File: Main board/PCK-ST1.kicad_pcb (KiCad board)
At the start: 4 copper layers, 65 x 55.6 mm, 195 parts, among them IC1 DRV8434/24, IC2 DRV8434/24, IC3 DRV8434/24, IC4 DRV8434/24, IC5 TLV70033DDCR, IC7 TPS2121RUXR, IC8 TPS25730DREFR, J1 RPi, J10 RA, J11 EL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

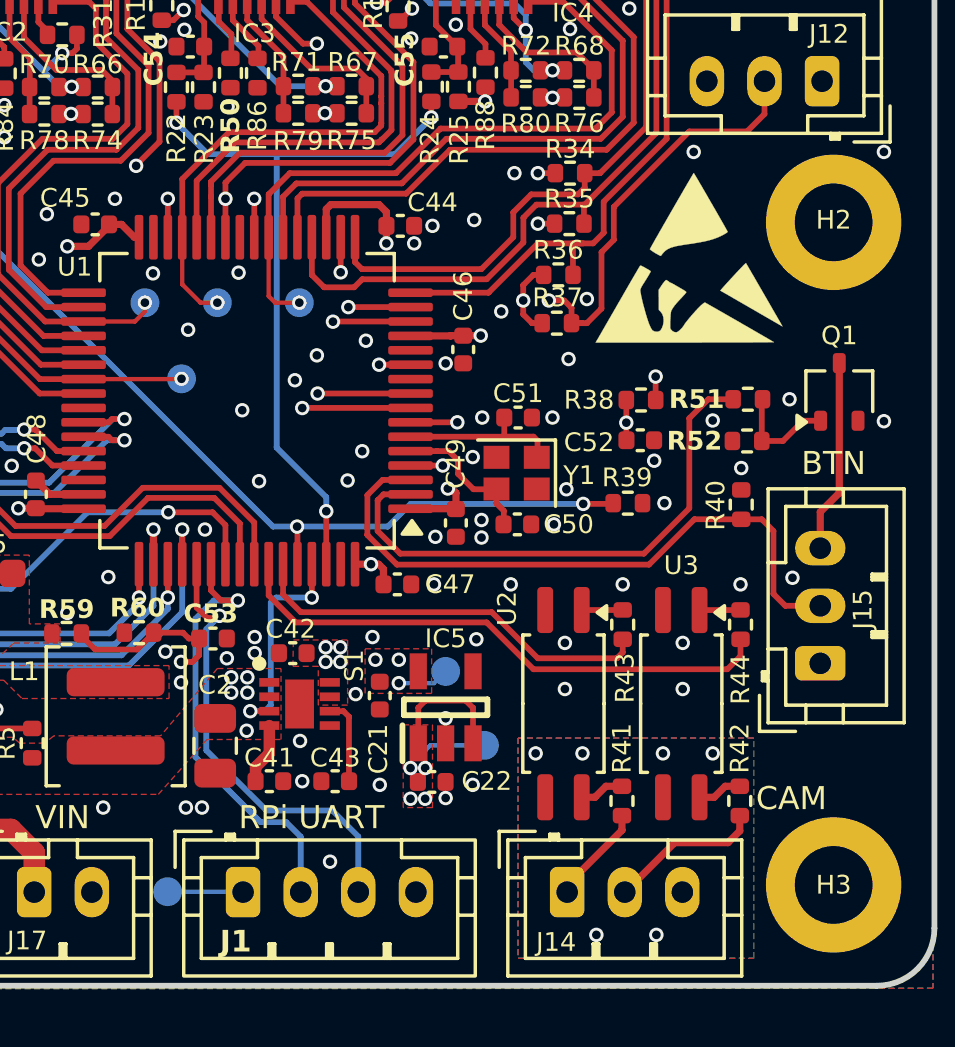
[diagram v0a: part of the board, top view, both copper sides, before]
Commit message: Added R1 pull-up to RPI_PWR_EN
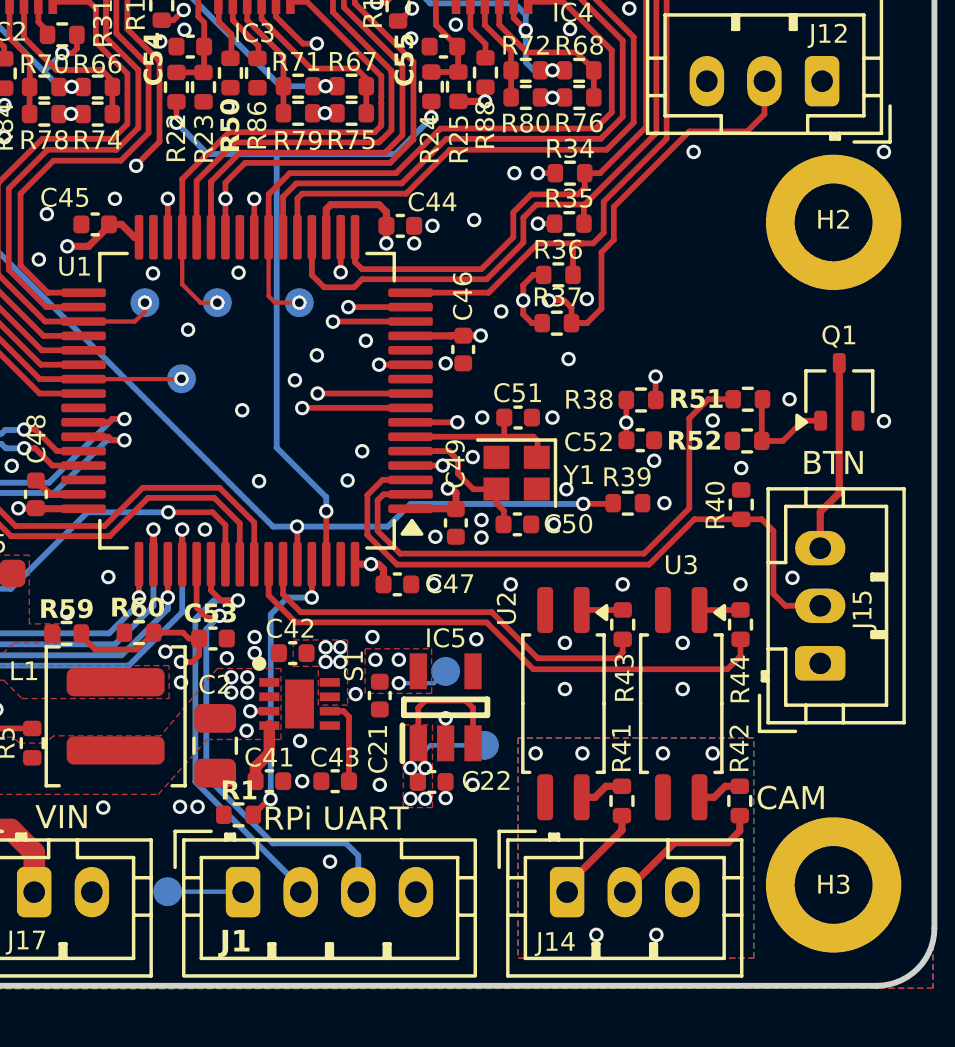
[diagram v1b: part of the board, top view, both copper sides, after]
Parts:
- removed REF**: ESD-Logo_6.6x6mm_SilkScreen, Symbol:ESD-Logo_6.6x6mm_SilkScreen
- added R1: 100k, Resistor_SMD:R_0402_1005Metric, F.Cu at (158.3, 109.1)
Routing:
- net /MCU/RPI_PWR_EN: track 7.71 -> 11.5 mm, vias 2 -> 3
- net /MCU/RPI_TX0: track 15.2 -> 14.7 mm
